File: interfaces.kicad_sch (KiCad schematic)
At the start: 35 parts, among them J3 Conn_01x15_Female, J4 Bus_M.2_Socket_E, Q1 BSS138APW, Q2 BSS138APW

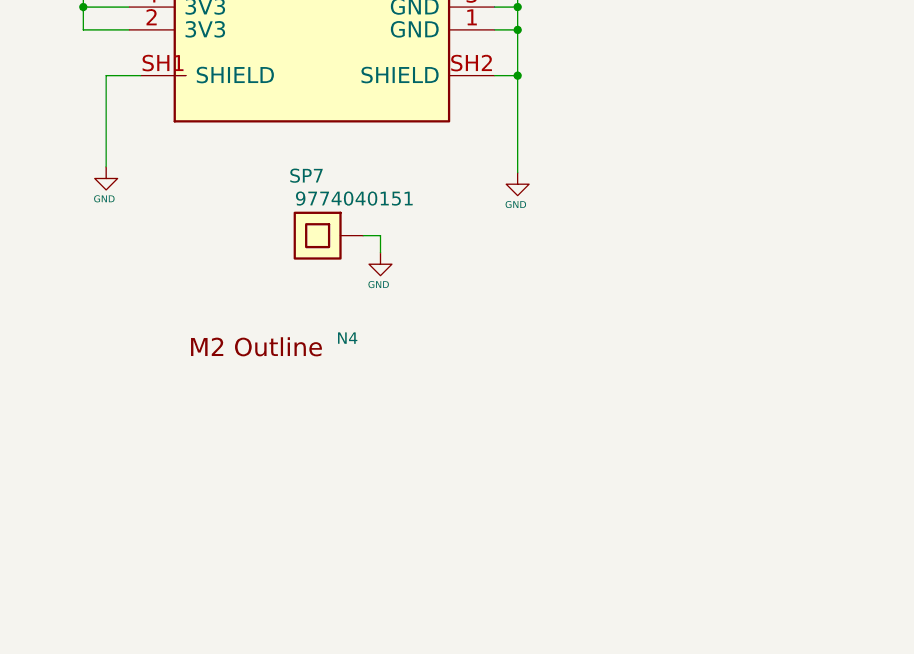
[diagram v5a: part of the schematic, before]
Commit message: Start of trigger FPGA.  Better layout
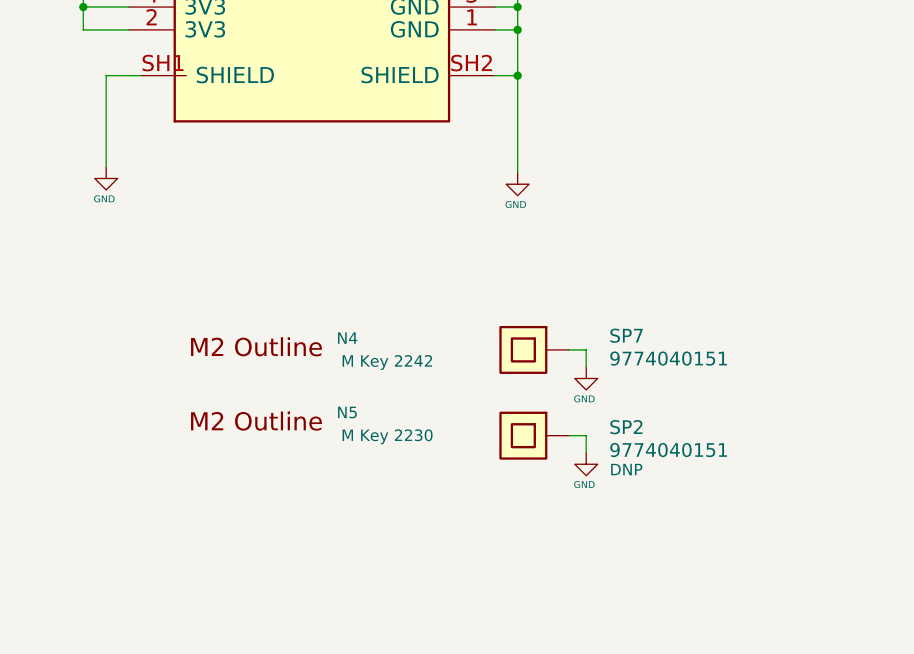
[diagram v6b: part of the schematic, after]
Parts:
- added N5: M Key 2230, jetson-nano-baseboard-footprints:M2outline-2230, symbol jetson-nano-baseboard:m2_outline
- added SP2: 9774040151, jetson-nano-baseboard-footprints:M2.5-4mm, symbol jetson-nano-baseboard:9774040151
- N4: value (none) -> M Key 2242; footprint (none) -> jetson-nano-baseboard-footprints:M2outline-2242
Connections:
- net GND: now also SP2.1
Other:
- moved on the sheet: SP7
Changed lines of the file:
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@@
+    (stroke (width 0) (type default) (color 0 0 0 0))
+  )
+  (wire (pts (xy 169.545 258.445) (xy 169.545 260.35))
     (stroke (width 0) (type default) (color 0 0 0 0))
   )
@@
     (stroke (width 0) (type default) (color 0 0 0 0))
   )
-  (wire (pts (xy 144.78 236.22) (xy 146.685 236.22))
+  (wire (pts (xy 167.64 248.92) (xy 169.545 248.92))
     (stroke (width 0) (type default) (color 0 0 0 0))
   )
@@
     (stroke (width 0) (type default) (color 0 0 0 0))
   )
+  (wire (pts (xy 167.64 258.445) (xy 169.545 258.445))
+    (stroke (width 0) (type default) (color 0 0 0 0))
+  )
   (wire (pts (xy 321.31 57.785) (xy 323.215 57.785))
     (stroke (width 0) (type default) (color 0 0 0 0))
@@
     (stroke (width 0) (type default) (color 0 0 0 0))
   )
-  (wire (pts (xy 146.685 236.22) (xy 146.685 238.125))
+  (wire (pts (xy 169.545 248.92) (xy 169.545 250.825))
     (stroke (width 0) (type default) (color 0 0 0 0))
   )
@@
     (pin "K")
   )
-  (symbol (lib_id "jetson-nano-baseboard:9774040151") (at 139.7 236.22 180) (unit 1)
-    (in_bom yes) (on_board yes)
-    (property "Reference" "SP7" (id 0) (at 136.525 230.505 0)
+  (symbol (lib_id "jetson-nano-baseboard:9774040151") (at 162.56 248.92 180) (unit 1)
+    (in_bom yes) (on_board yes)
+    (property "Reference" "SP7" (id 0) (at 172.085 248.285 0)
       (effects (font (size 1.524 1.524)) (justify right top))
     )
-    (property "Value" "9774040151" (id 1) (at 137.16 233.045 0)
+    (property "Value" "9774040151" (id 1) (at 172.085 250.825 0)
       (effects (font (size 1.524 1.524)) (justify right top))
     )
-    (property "Footprint" "jetson-nano-baseboard-footprints:M2.5-4mm" (id 2) (at 137.16 241.3 0)
-      (effects (font (size 1.524 1.524)) hide)
-    )
-    (property "Datasheet" "" (id 3) (at 137.16 241.3 0)
-      (effects (font (size 1.524 1.524)) hide)
-    )
-    (property "Manufacturer" "Wurth Elektronik" (id 4) (at 139.7 236.22 0)
-      (effects (font (size 1.27 1.27)) hide)
-    )
-    (property "MPN" "9774040151" (id 5) (at 139.7 236.22 0)
+    (property "Footprint" "jetson-nano-baseboard-footprints:M2.5-4mm" (id 2) (at 160.02 254 0)
+      (effects (font (size 1.524 1.524)) hide)
+    )
+    (property "Datasheet" "" (id 3) (at 160.02 254 0)
+      (effects (font (size 1.524 1.524)) hide)
+    )
+    (property "Manufacturer" "Wurth Elektronik" (id 4) (at 162.56 248.92 0)
+      (effects (font (size 1.27 1.27)) hide)
+    )
+    (property "MPN" "9774040151" (id 5) (at 162.56 248.92 0)
       (effects (font (size 1.27 1.27)) hide)
     )
@@
     (pin "SH2")
   )
-  (symbol (lib_id "jetson-nano-baseboard:GND") (at 146.685 238.125 0) (unit 1)
-    (in_bom yes) (on_board yes)
-    (property "Reference" "#GND_041" (id 0) (at 146.685 238.125 0)
+  (symbol (lib_id "jetson-nano-baseboard:GND") (at 169.545 250.825 0) (unit 1)
+    (in_bom yes) (on_board yes)
+    (property "Reference" "#GND_041" (id 0) (at 169.545 250.825 0)
       (effects (font (size 0.508 0.508)) hide)
     )
-    (property "Value" "GND" (id 1) (at 146.4818 241.681 0)
+    (property "Value" "GND" (id 1) (at 169.3418 254.381 0)
       (effects (font (size 0.762 0.762)))
     )
-    (property "Footprint" "" (id 2) (at 146.685 238.125 0)
-      (effects (font (size 1.778 1.778)) hide)
-    )
-    (property "Datasheet" "" (id 3) (at 146.685 238.125 0)
+    (property "Footprint" "" (id 2) (at 169.545 250.825 0)
+      (effects (font (size 1.778 1.778)) hide)
+    )
+    (property "Datasheet" "" (id 3) (at 169.545 250.825 0)
       (effects (font (size 1.778 1.778)) hide)
     )
@@
     (pin "1")
   )
+  (symbol (lib_id "jetson-nano-baseboard:9774040151") (at 162.56 258.445 180) (unit 1)
+    (in_bom yes) (on_board yes)
+    (property "Reference" "SP2" (id 0) (at 172.085 258.445 0)
+      (effects (font (size 1.524 1.524)) (justify right top))
+    )
+    (property "Value" "9774040151" (id 1) (at 172.085 260.985 0)
+      (effects (font (size 1.524 1.524)) (justify right top))
+    )
+    (property "Footprint" "jetson-nano-baseboard-footprints:M2.5-4mm" (id 2) (at 160.02 263.525 0)
+      (effects (font (size 1.524 1.524)) hide)
+    )
+    (property "Datasheet" "" (id 3) (at 160.02 263.525 0)
+      (effects (font (size 1.524 1.524)) hide)
+    )
+    (property "Manufacturer" "Wurth Elektronik" (id 4) (at 162.56 258.445 0)
+      (effects (font (size 1.27 1.27)) hide)
+    )
+    (property "MPN" "9774040151" (id 5) (at 162.56 258.445 0)
+      (effects (font (size 1.27 1.27)) hide)
+    )
+    (property "DNP" "DNP" (id 6) (at 173.99 262.255 0))
+    (pin "1")
+  )
   (symbol (lib_id "jetson-nano-baseboard:GND") (at 203.2 69.85 0) (unit 1)
     (in_bom yes) (on_board yes)
@@
     (pin "1")
     (pin "2")
+  )
+  (symbol (lib_id "jetson-nano-baseboard:GND") (at 169.545 260.35 0) (unit 1)
+    (in_bom yes) (on_board yes)
+    (property "Reference" "#GND_011" (id 0) (at 169.545 260.35 0)
+      (effects (font (size 0.508 0.508)) hide)
+    )
+    (property "Value" "GND" (id 1) (at 169.3418 263.906 0)
+      (effects (font (size 0.762 0.762)))
+    )
+    (property "Footprint" "" (id 2) (at 169.545 260.35 0)
+      (effects (font (size 1.778 1.778)) hide)
+    )
+    (property "Datasheet" "" (id 3) (at 169.545 260.35 0)
+      (effects (font (size 1.778 1.778)) hide)
+    )
+    (pin "1")
   )
   (symbol (lib_id "jetson-nano-baseboard:C_100n_0402") (at 291.465 139.7 90) (unit 1)
@@
     (pin "2")
     (pin "3")
+  )
+  (symbol (lib_id "jetson-nano-baseboard:m2_outline") (at 132.08 255.905 0) (unit 1)
+    (in_bom no) (on_board yes)
+    (property "Reference" "N5" (id 0) (at 143.002 255.905 0))
+    (property "Value" "M Key 2230" (id 1) (at 147.447 258.445 0))
+    (property "Footprint" "jetson-nano-baseboard-footprints:M2outline-2230" (id 2) (at 132.588 262.001 0)
+      (effects (font (size 1.27 1.27)) hide)
+    )
+    (property "Datasheet" "" (id 3) (at 132.08 255.905 0)
+      (effects (font (size 1.27 1.27)) hide)
+    )
   )
   (symbol (lib_id "jetson-nano-baseboard:m2_outline") (at 327.025 237.49 0) (unit 1)
@@
     (in_bom no) (on_board yes)
     (property "Reference" "N4" (id 0) (at 143.002 247.65 0))
-    (property "Value" "" (id 1) (at 147.447 250.19 0))
-    (property "Footprint" "" (id 2) (at 132.588 253.746 0)
-      (effects (font (size 1.27 1.27)) hide)
-    )
+    (property "Value" "M Key 2242" (id 1) (at 147.447 250.19 0))
+    (property "Footprint" "jetson-nano-baseboard-footprints:M2outline-2242" (id 2) (at 132.588 253.746 0)
+      (effects (font (size 1.27 1.27)) hide)
+    )

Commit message: Checkpoint
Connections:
- net UART0_RXD: now reaches J4.22 (UART_RXD)
- net UART0_TXD: now reaches J4.32 (UART_TXD)
- net UART0_CTS: now reaches J4.34 (UART_CTS)
- net UART0_RTS: now reaches J4.36 (UART_RTS)
- no-connect marks 37 -> 39
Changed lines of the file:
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@@
   (no_connect (at 227.33 55.88))
   (no_connect (at 118.745 180.34))
+  (no_connect (at 304.8 210.82))
+  (no_connect (at 304.8 213.36))
   (no_connect (at 159.385 134.62))
   (no_connect (at 118.745 187.96))
@@
     (stroke (width 0) (type default) (color 0 0 0 0))
   )
+  (wire (pts (xy 355.6 185.42) (xy 365.76 185.42))
+    (stroke (width 0) (type default) (color 0 0 0 0))
+  )
   (wire (pts (xy 161.925 142.24) (xy 161.925 149.86))
     (stroke (width 0) (type default) (color 0 0 0 0))
@@
     (stroke (width 0) (type default) (color 0 0 0 0))
   )
+  (wire (pts (xy 355.6 177.8) (xy 365.76 177.8))
+    (stroke (width 0) (type default) (color 0 0 0 0))
+  )
   (wire (pts (xy 101.6 120.65) (xy 101.6 131.445))
     (stroke (width 0) (type default) (color 0 0 0 0))
@@
     (stroke (width 0) (type default) (color 0 0 0 0))
   )
+  (wire (pts (xy 355.6 182.88) (xy 365.76 182.88))
+    (stroke (width 0) (type default) (color 0 0 0 0))
+  )
   (wire (pts (xy 167.64 248.92) (xy 169.545 248.92))
     (stroke (width 0) (type default) (color 0 0 0 0))
@@
   )
   (wire (pts (xy 159.385 157.48) (xy 161.925 157.48))
+    (stroke (width 0) (type default) (color 0 0 0 0))
+  )
+  (wire (pts (xy 355.6 180.34) (xy 365.76 180.34))
     (stroke (width 0) (type default) (color 0 0 0 0))
   )
@@
     )
   )
+  (global_label "UART0_CTS" (shape output) (at 365.76 182.88 0) (fields_autoplaced)
+    (effects (font (size 1.27 1.27)) (justify left))
+    (property "Intersheet References" "${INTERSHEET_REFS}" (id 0) (at 378.3652 182.8006 0)
+      (effects (font (size 1.27 1.27)) (justify left) hide)
+    )
+  )
   (global_label "PCIE0_TX1_P" (shape input) (at 212.725 167.64 0) (fields_autoplaced)
     (effects (font (size 1.27 1.27)) (justify left))
@@
     )
   )
+  (global_label "UART0_RTS" (shape input) (at 365.76 185.42 0) (fields_autoplaced)
+    (effects (font (size 1.27 1.27)) (justify left))
+    (property "Intersheet References" "${INTERSHEET_REFS}" (id 0) (at 378.3652 185.3406 0)
+      (effects (font (size 1.27 1.27)) (justify left) hide)
+    )
+  )
   (global_label "W_DISABLE1_CTRL" (shape input) (at 377.825 57.785 0) (fields_autoplaced)
     (effects (font (size 1.27 1.27)) (justify left))
@@
     )
   )
+  (global_label "UART0_RXD" (shape output) (at 365.76 177.8 0) (fields_autoplaced)
+    (effects (font (size 1.27 1.27)) (justify left))
+    (property "Intersheet References" "${INTERSHEET_REFS}" (id 0) (at 378.6675 177.7206 0)
+      (effects (font (size 1.27 1.27)) (justify left) hide)
+    )
+  )
   (global_label "I2C2_SDA" (shape input) (at 380.365 142.24 0) (fields_autoplaced)
     (effects (font (size 1.27 1.27)) (justify left))
@@
     )
   )
+  (global_label "UART0_TXD" (shape input) (at 365.76 180.34 0) (fields_autoplaced)
+    (effects (font (size 1.27 1.27)) (justify left))
+    (property "Intersheet References" "${INTERSHEET_REFS}" (id 0) (at 378.3652 180.2606 0)
+      (effects (font (size 1.27 1.27)) (justify left) hide)
+    )
+  )

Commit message: Checkpoint
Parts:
- added J16: Conn_02x12_Odd_Even, capablerobot-footprints:DF40C-24DP-0.4V51, symbol Connector_Generic:Conn_02x12_Odd_Even
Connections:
- net 3V3_SYS: now also J16.19 (Pin_19)
- net GND: now also J16.14 (Pin_14), J16.2 (Pin_2), J16.20 (Pin_20), J16.8 (Pin_8)
- net USB2_D_N: now also D4.2 (IO2); no longer D4.1 (IO1)
- net USB2_D_P: now also D4.1 (IO1); no longer D4.2 (IO2)
- new net I2C1_SCL: J16.3 (Pin_3)
- new net I2C1_SDA: J16.1 (Pin_1)
- new net UART1_CTS: J16.5 (Pin_5)
- new net UART1_RTS: J16.7 (Pin_7)
- new net UART1_RXD: J16.9 (Pin_9)
- new net UART1_TXD: J16.11 (Pin_11)
- new net USB_VBUS: J16.22 (Pin_22), J16.24 (Pin_24)
